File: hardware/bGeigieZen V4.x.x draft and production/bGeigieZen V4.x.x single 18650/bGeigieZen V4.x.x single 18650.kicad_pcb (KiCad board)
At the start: 2 copper layers, 129.4 x 64.6 mm, 10 parts, among them J1 M5 2x15 pin, J2 Geiger IRover, J3 GPS, J4 Geiger Safepulse, J5 Extra support header

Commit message: V4.0.5 boards updates
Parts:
- moved G front 61.9 mm to (93.5, 97.2)
- moved J3 27.7 mm to (209.2, 79.3), turned to 0 degrees
- moved J4 12.8 mm to (186.9, 87.1)
- moved J5 12.8 mm to (157.0, 103.6)
- moved J1 11.2 mm to (150.4, 114.4)
- moved H4 11.2 mm to (110.5, 75.9)
- moved H6 11.2 mm to (110.7, 119.6)
- moved J2 7.85 mm to (201.5, 92.8)
- moved BT1 1.04 mm to (173.8, 76.7)
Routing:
- net /SDA: track 75.1 -> 93.7 mm
- net /TX2: track 77.2 -> 93.2 mm, vias 0 -> 1
- net /GIO2 on Core and GIO32 on Core-2: track 108.5 -> 93.2 mm, vias 0 -> 1
- net 3.3V: track 102.3 -> 87.4 mm
- net /RX2: track 75.8 -> 89.7 mm, vias 1 -> 0
- net /SCL: track 81.9 -> 95.2 mm
- net /BAT: track 117.8 -> 105.8 mm

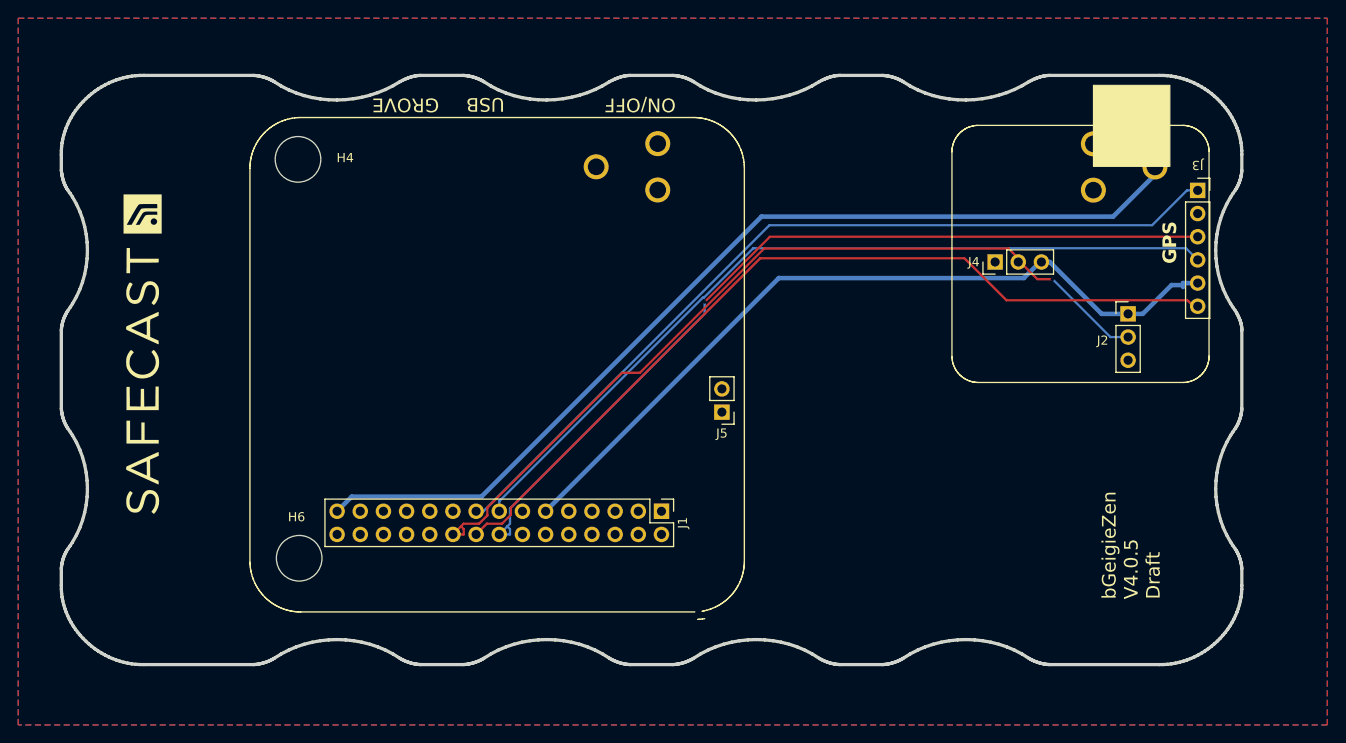
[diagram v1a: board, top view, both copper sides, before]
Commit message: reverses axp192 power setup (mistake)
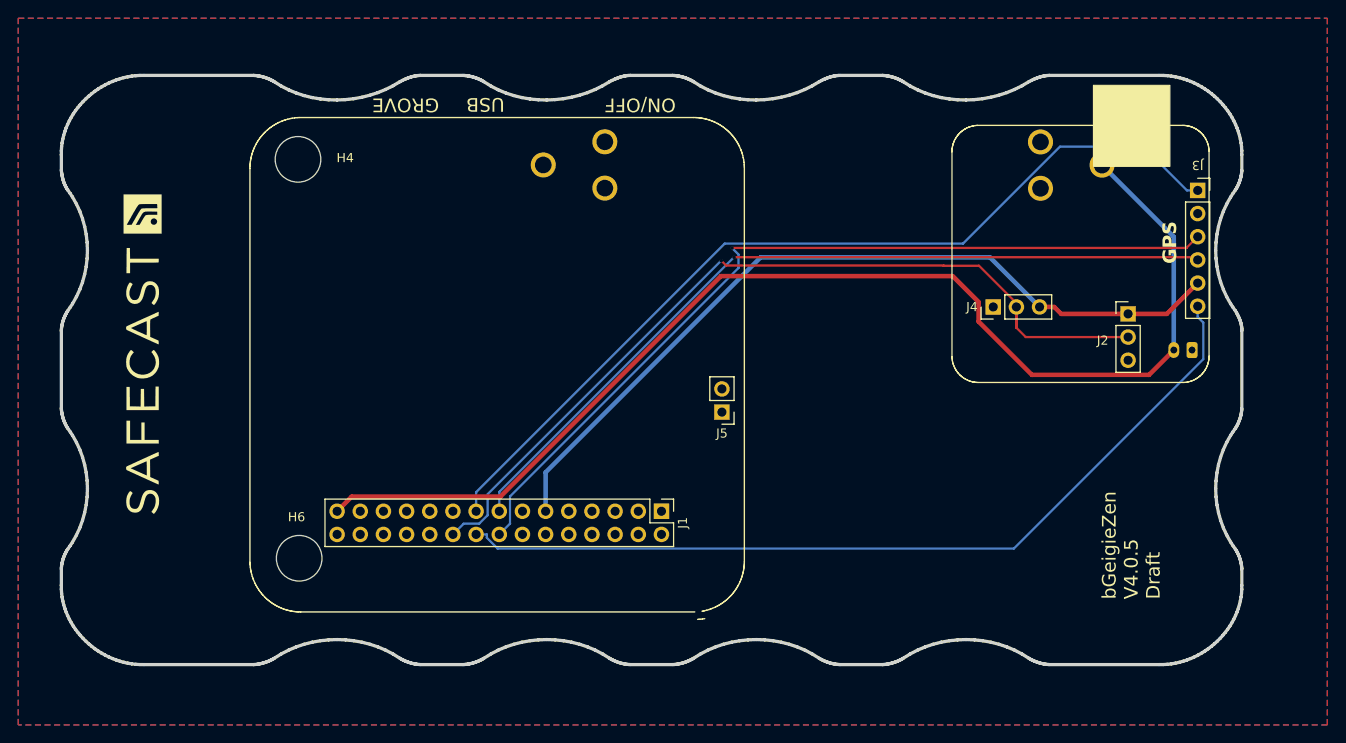
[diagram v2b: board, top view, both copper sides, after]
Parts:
- added QI: QI GND, Connector_JST:JST_PH_B2B-PH-K_1x02_P2.00mm_Vertical, B.Cu at (208.5, 96.8)
- moved G back 54.4 mm to (138.0, 124.0), turned to 0 degrees
- moved BT1 5.80 mm to (168.0, 76.5)
- moved J4 4.93 mm to (186.7, 92.0)
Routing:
- net /BAT: track 105.8 -> 132.8 mm
- net /SDA: track 93.7 -> 98.9 mm
- net 3.3V: track 87.4 -> 89.5 mm
- net /GIO2 on Core and GIO32 on Core-2: track 93.2 -> 95.1 mm
- net /TX2: track 93.2 -> 94.1 mm
- net /RX2: track 89.7 -> 89.5 mm, vias 0 -> 1

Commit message: Added grid and V4.0.5 boards
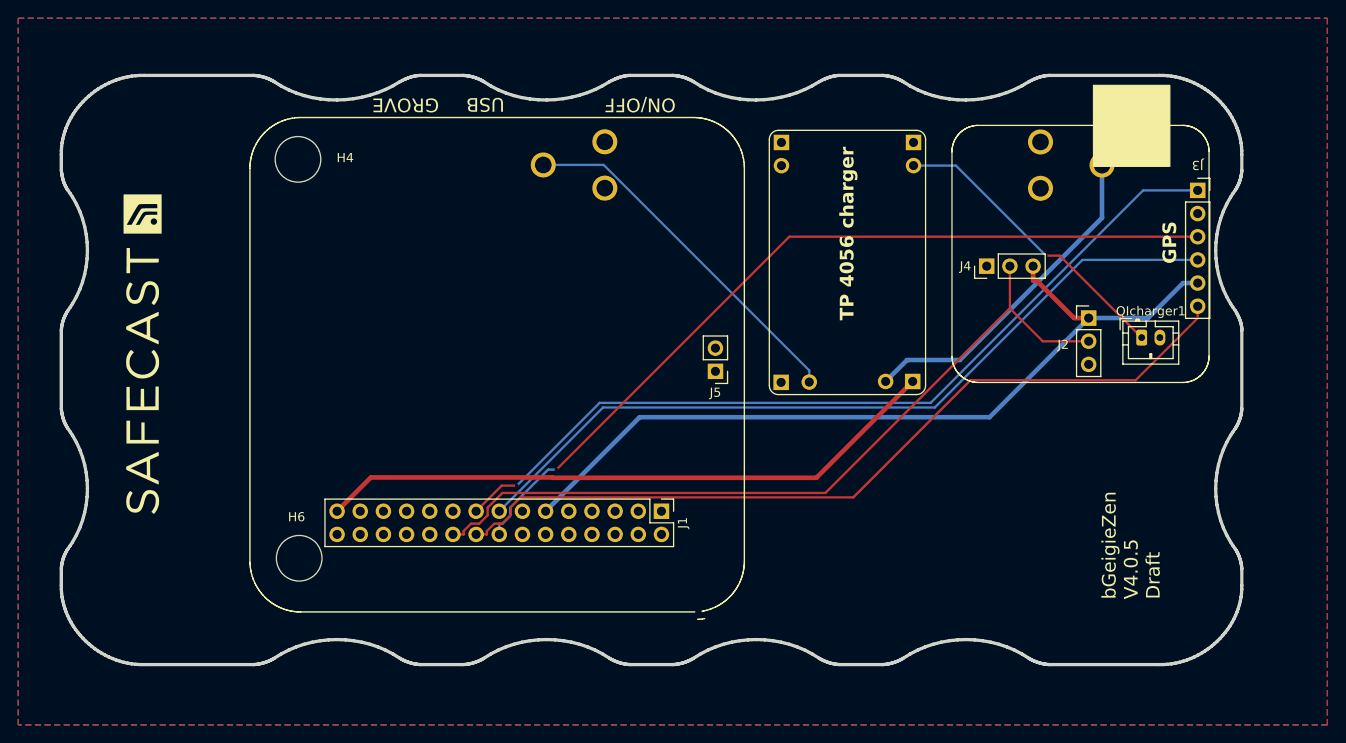
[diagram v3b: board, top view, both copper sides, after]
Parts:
- removed QI: QI GND, Connector_JST:JST_PH_B2B-PH-K_1x02_P2.00mm_Vertical
- added QIcharger1: QI GND, Connector_JST:JST_PH_B2B-PH-K_1x02_P2.00mm_Vertical, F.Cu at (203.0, 95.4)
- added TP4056: TP4056, bGeigieZen:TP4056, F.Cu at (170.8, 87.7)
- moved G back 51.9 mm to (93.5, 97.2), turned to -90 degrees
- moved J4 4.53 mm to (186.0, 87.6)
- moved J5 4.53 mm to (156.3, 99.1)
- moved J2 4.34 mm to (197.2, 93.3)
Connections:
- BT1 pad 1: /BAT -> Net-(BT1-+)
- BT1 pad 2: GND -> Net-(BT1--)
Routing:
- net /BAT: track 132.8 -> 69.0 mm
- net Net-(BT1--): track 0.00 -> 39.8 mm
- net Net-(BT1-+): track 0.00 -> 36.9 mm
- net Net-(QIcharger1-Pin_1): track 0.00 -> 32.8 mm, vias 0 -> 1
- net /GIO2 on Core and GIO32 on Core-2: track 95.1 -> 86.8 mm, vias 1 -> 0
- net /SDA: track 98.9 -> 93.7 mm, vias 0 -> 1
- net /SCL: track 95.2 -> 90.9 mm
- net /TX2: track 94.1 -> 91.3 mm
- net 3.3V: track 89.5 -> 91.2 mm
- net /RX2: track 89.5 -> 88.0 mm, vias 1 -> 0

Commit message: Modified V4.0.5 board graphics
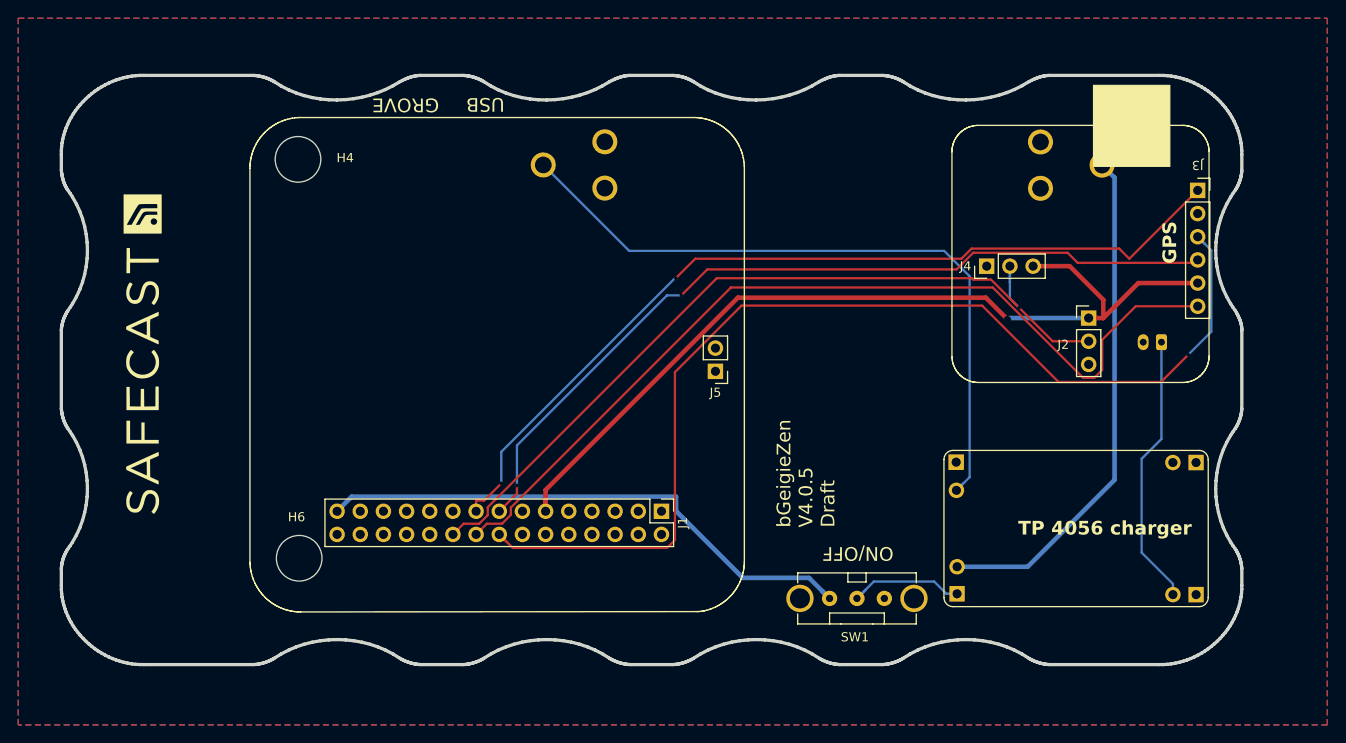
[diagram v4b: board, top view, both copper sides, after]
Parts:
- added G***: LOGO, bGeigieRaku_M5_1015:18650 map, B.Cu at (160.9, 76.4)
- added SW1: SW_SPDT, bGeigieRaku_M5_1015:EG1206, F.Cu at (171.8, 124.0)
- QIcharger1: moved to B.Cu
- moved TP4056 37.7 mm to (195.3, 116.4), turned to -90 degrees
- moved QIcharger1 2.23 mm to (205.2, 95.9), turned to 180 degrees
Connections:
- TP4056 pad 4: /BAT -> Net-(SW1-B)
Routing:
- net Net-(BT1--): track 39.8 -> 76.9 mm
- net /TX2: track 91.3 -> 119.3 mm
- net Net-(BT1-+): track 36.9 -> 57.2 mm
- net Net-(SW1-B): track 0.00 -> 13.6 mm
- net /SCL: track 90.9 -> 100.1 mm
- net /BAT: track 69.0 -> 61.3 mm
- net 3.3V: track 91.2 -> 97.6 mm, vias 0 -> 1
- net /GIO2 on Core and GIO32 on Core-2: track 86.8 -> 92.3 mm, vias 0 -> 1
- net /RX2: track 88.0 -> 92.2 mm, vias 0 -> 2
- net /SDA: track 93.7 -> 97.3 mm, vias 1 -> 2
- net Net-(QIcharger1-Pin_1): track 32.8 -> 30.6 mm, vias 1 -> 0

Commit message: Date and graphic changes
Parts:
- renumbered QIcharger1 to QI
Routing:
- net Net-(QIcharger1-Pin_1): track 30.6 -> 32.0 mm
- net 3.3V: track 97.6 -> 98.7 mm
- net /SDA: track 97.3 -> 96.4 mm
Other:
- board text added: "Irover"
- board text added: "M5StackCore"
- board text added: "ON OFF"
- board text added: "SDcard"
